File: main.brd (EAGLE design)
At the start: 81 x 58.4 mm, 23 parts, among them IC1 SN754410, IC2 7805T, T1 BP103, T2 BP103, T3 BP103

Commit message: Changed Teensy 3.2 to Teensy 2.0
Also changed switches to pull down on press, using pull up resistors on
teensy.
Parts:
- removed R7, R8: 10k, resistor-power:RS1/4
- added LED4: (no value), led:LED3MM
- added R10: 1.8K, resistor-power:RS1/4
- added R9: 120, resistor-power:RS1/4
- added T4: BP103, opto-trans-siemens:BP103
- added _1: TEENSY, teensy:TEENSY
- renumbered SG1 to BUZZER, U$1 to TEENSY
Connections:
- new net 5V: _1.+5V
- new net L4: R9.2, TEENSY.13
- new net N$9: LED4.A, R9.1
- new net T4: R10.1, T4.C, TEENSY.17/A3
- new net _5V2: _1.5V2
- new net _B0: _1.B0
- new net _B1: _1.B1
- new net _B2: _1.B2
- new net _B3: _1.B3
- new net _B4: _1.B4
- new net _B5: _1.B5
- new net _B6: _1.B6
- new net _B7: _1.B7
- new net _C7: _1.C7
- new net _D0: _1.D0
- new net _D1: _1.D1
- new net _D2: _1.D2
- new net _D3: _1.D3
- new net _D4: _1.D4
- new net _D5: _1.D5
- new net _D6: _1.D6
- new net _D7: _1.D7
- new net _E6: _1.E6
- new net _F0: _1.F0
- new net _F1: _1.F1
- new net _F4: _1.F4
- new net _F5: _1.F5
- new net _F6: _1.F6
- new net _F7: _1.F7
- new net _RST: _1.RST
- net +3V3: no longer S1.1, S1.2, S2.1, S2.2
- net +5V: now also R10.2
- net GND: now also LED4.K, S1.1, S1.2, S2.1, S2.2, T4.E, _1.GND; no longer R7.1, R8.1
- net L1: now also TEENSY.10; no longer TEENSY.17/A3
- net L2: now also TEENSY.11; no longer TEENSY.18/A4
- net L3: now also TEENSY.12; no longer TEENSY.19/A5
- net S1: no longer R7.2
- net S2: no longer R8.2
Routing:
- net +3V3: track 118.1 -> 68.5 mm
- net GND: track 8.15 -> 34.9 mm
- net S2: track 52.2 -> 27.6 mm
- net S1: track 64.3 -> 47.8 mm
- net L3: track 8.98 -> 0.00 mm
- net L1: track 16.7 -> 15.6 mm
- net L2: track 12.1 -> 10.9 mm

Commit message: Made schematic and board consistent
Also changed transistor package
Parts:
- removed _1: TEENSY, teensy:TEENSY
- LED1, LED2, LED3, LED4: value (none) -> 950
- S1, S2: value (none) -> 0
- T1, T2, T3, T4: value BP103 -> BPX81; device opto-trans-siemens:BP103 -> opto-trans-siemens:BPX81
- TEENSY: value TEENSY_3.1-3.2_DIL -> TEENSY; device Teensy_3_and_LC_Series_Boards_v1.4:TEENSY_3.0-3.2&LC_DIL -> teensy:TEENSY
- moved T4 54.0 mm to (44.5, 11.4)
- moved T1 50.0 mm to (54.6, 3.81), turned to 0 degrees
- moved T2 28.8 mm to (54.6, 8.89), turned to 0 degrees
- moved T3 24.1 mm to (49.5, 8.89), turned to 0 degrees
- turned TEENSY to 90 degrees
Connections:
- removed net +3V3: J_ENCODER_1.VCC, J_ENCODER_2.VCC, TEENSY.3.3V
- removed net 5V: _1.+5V
- removed net AGND: TEENSY.AGND
- removed net _5V2: _1.5V2
- removed net _B0: _1.B0
- removed net _B1: _1.B1
- removed net _B2: _1.B2
- removed net _B3: _1.B3
- removed net _B4: _1.B4
- removed net _B5: _1.B5
- removed net _B6: _1.B6
- removed net _B7: _1.B7
- removed net _C7: _1.C7
- removed net _D0: _1.D0
- removed net _D1: _1.D1
- removed net _D2: _1.D2
- removed net _D3: _1.D3
- removed net _D4: _1.D4
- removed net _D5: _1.D5
- removed net _D6: _1.D6
- removed net _D7: _1.D7
- removed net _E6: _1.E6
- removed net _F0: _1.F0
- removed net _F1: _1.F1
- removed net _F4: _1.F4
- removed net _F5: _1.F5
- removed net _F6: _1.F6
- removed net _F7: _1.F7
- removed net _RST: _1.RST
- net +5V: now also J_ENCODER_1.VCC, J_ENCODER_2.VCC, TEENSY.+5V; no longer TEENSY.VIN
- net BZ: now also TEENSY.B3; no longer TEENSY.6
- net GND: no longer _1.GND
- net L1: now also TEENSY.B0; no longer TEENSY.10
- net L2: now also TEENSY.B1; no longer TEENSY.11
- net L3: now also TEENSY.B2; no longer TEENSY.12
- net L4: now also TEENSY.D1; no longer TEENSY.13
- net M1E: now also TEENSY.B7; no longer TEENSY.20/A6
- net M1F: now also TEENSY.D2; no longer TEENSY.2
- net M1R: now also TEENSY.D3; no longer TEENSY.3
- net M2E: now also TEENSY.D0; no longer TEENSY.21/A7
- net M2F: now also TEENSY.D6; no longer TEENSY.4
- net M2R: now also TEENSY.D7; no longer TEENSY.5
- net S1: now also TEENSY.B4; no longer TEENSY.22/A8
- net S2: now also TEENSY.B5; no longer TEENSY.23/A9
- net T1: now also TEENSY.F0; no longer TEENSY.14/A0
- net T2: now also TEENSY.F1; no longer TEENSY.15/A1
- net T3: now also TEENSY.F4; no longer TEENSY.16/A2
- net T4: now also TEENSY.F5; no longer TEENSY.17/A3
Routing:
- net +5V: track 126.1 -> 0.00 mm
- net +3V3: track 68.5 -> 0.00 mm
- net M1E: track 52.3 -> 0.00 mm
- net N$2: track 49.0 -> 0.00 mm
- net S1: track 47.8 -> 0.00 mm
- net T1: track 47.5 -> 0.00 mm
- net N$3: track 42.2 -> 0.00 mm
- net N$5: track 38.5 -> 0.00 mm
- net M2F: track 35.7 -> 0.00 mm
- net GND: track 34.9 -> 0.00 mm
- net N$4: track 32.7 -> 0.00 mm
- net M2E: track 31.6 -> 0.00 mm
- net M1F: track 30.8 -> 0.00 mm
- net T3: track 28.1 -> 0.00 mm
- net T2: track 27.9 -> 0.00 mm
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
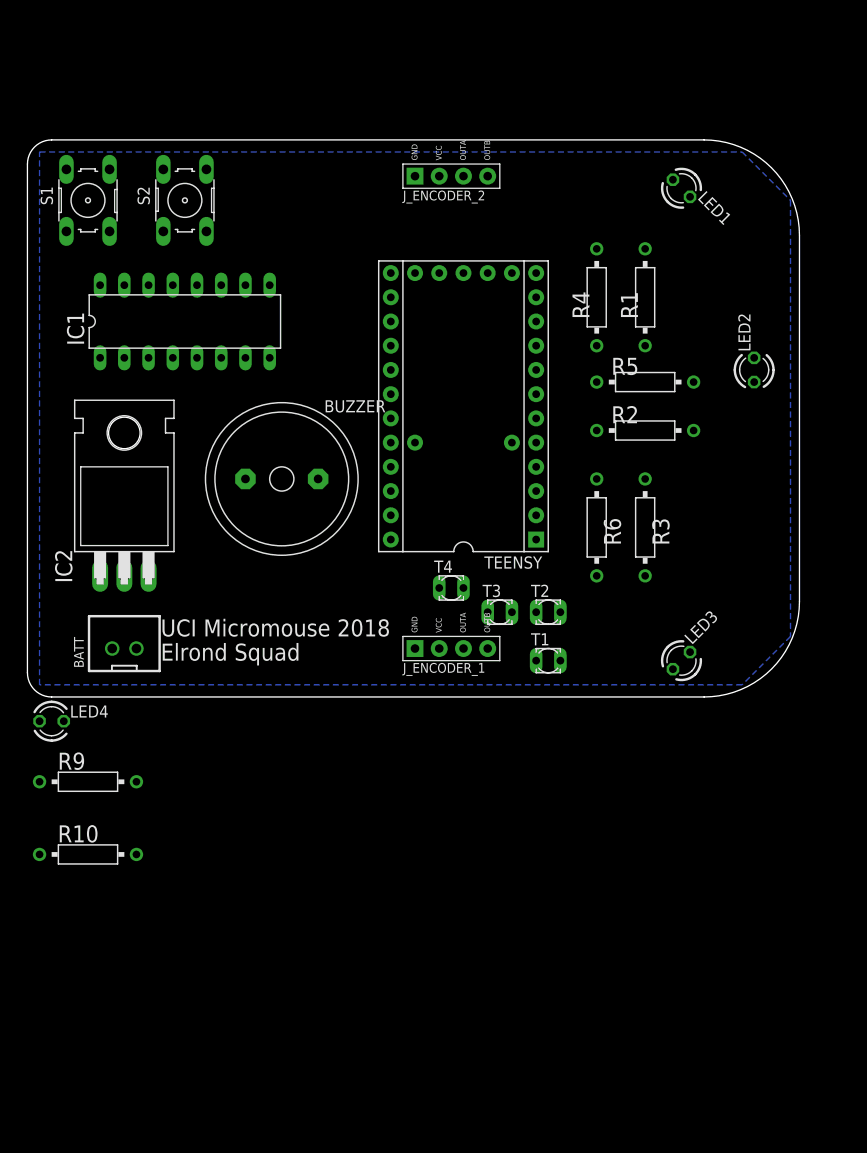
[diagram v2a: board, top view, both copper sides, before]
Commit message: Laid out components on PCB
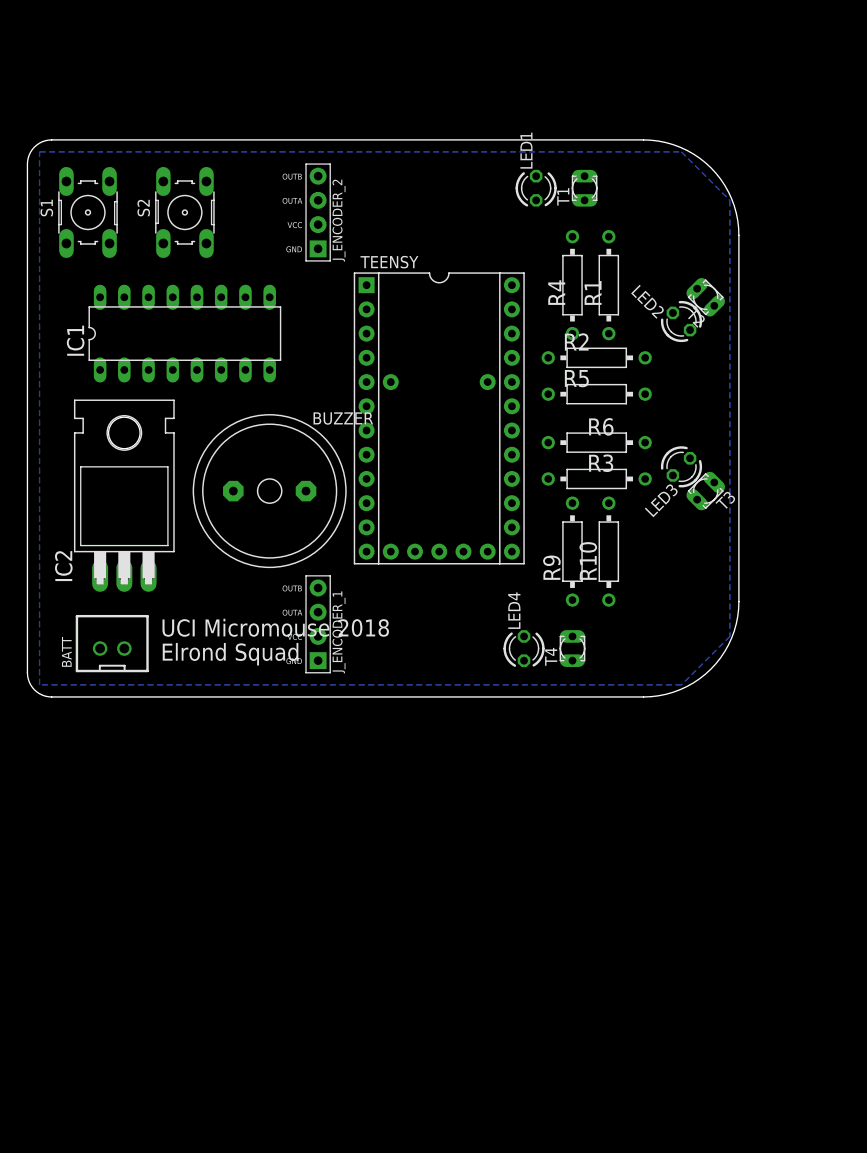
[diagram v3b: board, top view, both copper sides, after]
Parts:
- moved R10 63.2 mm to (61.0, 15.2), turned to 90 degrees
- moved R9 56.2 mm to (57.1, 15.2), turned to 90 degrees
- moved LED4 50.1 mm to (52.1, 5.08), turned to 90 degrees
- moved T1 49.7 mm to (58.4, 53.3), turned to 90 degrees
- moved T2 36.9 mm to (71.1, 41.9), turned to 135 degrees
- moved T3 25.0 mm to (71.1, 21.6), turned to 225 degrees
- moved LED3 20.3 mm to (68.6, 24.1), turned to 225 degrees
- moved LED1 15.2 mm to (53.3, 53.3), turned to 90 degrees
- moved J_ENCODER_2 14.5 mm to (30.5, 50.8), turned to 90 degrees
- moved J_ENCODER_1 14.2 mm to (30.5, 7.62), turned to 90 degrees
- moved T4 14.2 mm to (57.1, 5.08), turned to 90 degrees
- moved LED2 9.16 mm to (68.6, 39.4), turned to 135 degrees
- moved R2 9.16 mm to (59.7, 35.6)
- moved R6 8.89 mm to (59.7, 26.7), turned to 180 degrees
- moved R3 7.18 mm to (59.7, 22.9), turned to 180 degrees
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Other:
- board size 81 x 58.4 mm -> 74.6 x 58.4 mm

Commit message: Peer Review Version
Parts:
- removed J_ENCODER_1, J_ENCODER_2: ENCODER, Pololu Encoder and Motor Driver:ENCODER_FOOTPRINT
- added S3: (no value), switch:255SB
- added SV1, SV2: (no value), con-lstb:MA06-1
- added U$1, U$2: POLULUMOTOR, personal:FP
- added U$3: CASTERBALL, personal:FB_CASTER
- moved BUZZER 37.7 mm to (8.01, 55.0), turned to 90 degrees
- moved LED1 27.7 mm to (78.0, 66.0), turned to 135 degrees
- moved LED4 26.0 mm to (78.0, 4.00), turned to 225 degrees
- moved T1 25.1 mm to (82.0, 62.0), turned to 135 degrees
- moved T4 25.0 mm to (82.0, 8.00), turned to 225 degrees
- moved IC2 23.1 mm to (27.0, 7.00), turned to 270 degrees
- moved IC1 20.0 mm to (30.5, 53.6)
- moved S2 20.0 mm to (30.4, 65.3), turned to 0 degrees
- moved S1 18.1 mm to (17.4, 65.2), turned to 0 degrees
- moved R4 17.8 mm to (67.0, 58.0), turned to 180 degrees
- moved LED2 17.3 mm to (83.0, 49.0), turned to 270 degrees
- moved R2 16.9 mm to (73.0, 46.0)
- moved R5 15.7 mm to (73.0, 40.0)
- moved R1 14.9 mm to (73.0, 52.0), turned to 180 degrees
- moved LED3 14.8 mm to (83.0, 21.0), turned to 90 degrees
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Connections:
- removed net L3: R6.2, TEENSY.B2
- removed net L4: R9.2, TEENSY.D1
- removed net N$2: IC1.3, J_ENCODER_1.OUTA
- removed net N$3: IC1.6, J_ENCODER_1.OUTB
- removed net N$4: IC1.11, J_ENCODER_2.OUTB
- removed net N$5: IC1.14, J_ENCODER_2.OUTA
- new net ENC1A: SV1.3, TEENSY.F7
- new net ENC1B: SV1.2, TEENSY.F6
- new net ENC2A: SV2.3, TEENSY.B2
- new net ENC2B: SV2.2, TEENSY.B6
- new net M1A: IC1.3, SV1.6
- new net M1B: IC1.6, SV1.5
- new net M2A: IC1.14, SV2.6
- new net M2B: IC1.11, SV2.5
- new net N$10: IC2.3, S3.2
- new net VM1: SV1.4
- new net VM2: SV2.4
- net +5V: now also S3.3; no longer IC2.3, J_ENCODER_1.VCC, J_ENCODER_2.VCC
- net GND: now also SV1.1, SV2.1; no longer J_ENCODER_1.GND, J_ENCODER_2.GND
- net L1: now also R9.2
- net L2: now also R6.2
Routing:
- removed copper zone on layer 16, net GND
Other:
- board size 74.6 x 58.4 mm -> 86 x 70 mm
- board text removed: "Elrond Squad"
- board text removed: "UCI Micromouse 2018"

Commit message: Final artistic touches
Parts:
- moved BATT 1.60 mm to (8.00, 18.0)
- moved IC1 1.47 mm to (30.0, 55.0)
- moved BUZZER 1.44 mm to (9.00, 54.0)
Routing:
- net GND: track 0.00 -> 287.8 mm
- net +5V: track 0.00 -> 153.9 mm
- net T1: track 0.00 -> 104.3 mm
- net M2A: track 0.00 -> 79.9 mm
- net T2: track 0.00 -> 79.5 mm
- net T4: track 0.00 -> 78.0 mm
- net L1: track 0.00 -> 76.6 mm
- net M2B: track 0.00 -> 66.5 mm
- net T3: track 0.00 -> 66.3 mm
- net BZ: track 0.00 -> 47.9 mm
- net ENC1A: track 0.00 -> 46.3 mm
- net ENC1B: track 0.00 -> 45.3 mm
- net L2: track 0.00 -> 44.5 mm
- net ENC2B: track 0.00 -> 43.6 mm
- net M1A: track 0.00 -> 38.7 mm
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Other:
- board text added: "Micah, JD, John, Phuc, Jacob, Carlton"
- board text added: "Micromouse 2018 Elrond Squad"
